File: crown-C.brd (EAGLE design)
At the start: 57.8 x 50.8 mm, 85 parts

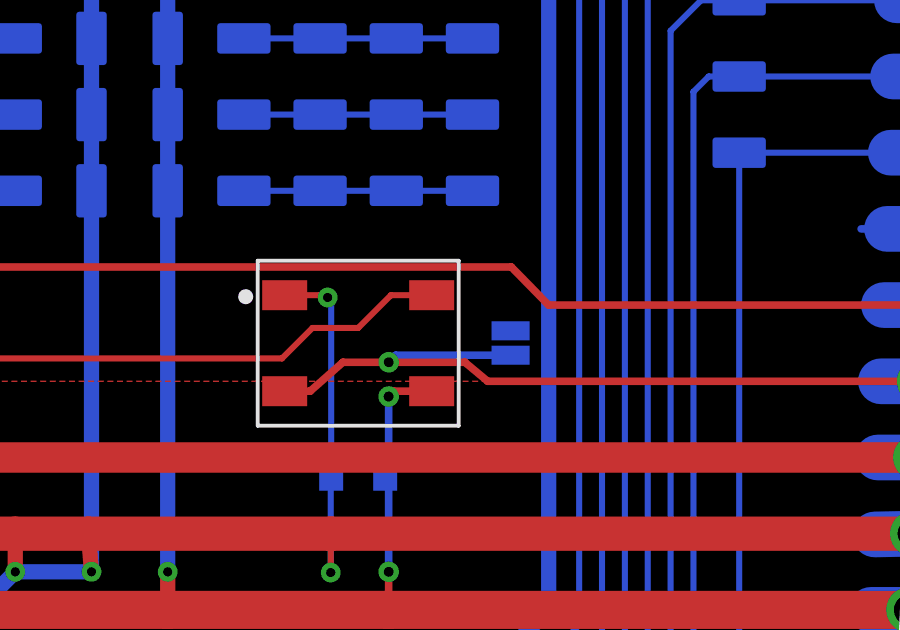
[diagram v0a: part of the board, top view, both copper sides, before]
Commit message: forgot a connection on skip-smd bits
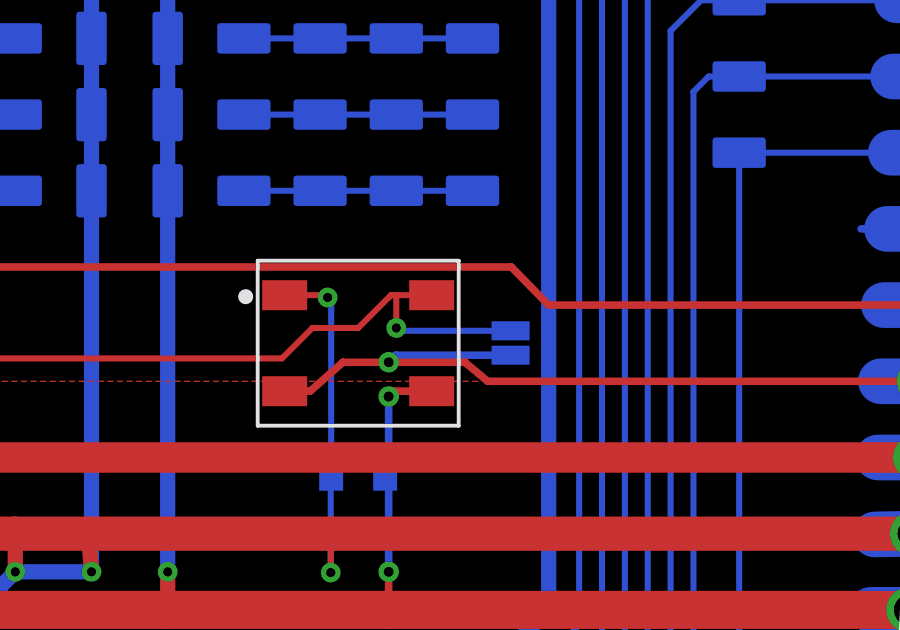
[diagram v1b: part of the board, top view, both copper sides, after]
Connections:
- net N$10: now also SKIP-SMD2.2
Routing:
- net N$10: track 28.2 -> 33.2 mm, vias 1 -> 2

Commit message: fixed incorrect resistor value
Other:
- board text added: "PIXEL LINE TERMINATION (500 OHM RES)"
- board text removed: "PIXEL LINE TERMINATION (150 OHM RES)"
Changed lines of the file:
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@@
 <text x="12.954" y="16.51" size="0.762" layer="22" font="vector" ratio="15" rot="MR90" align="bottom-center">PIXEL LINE
 TERMINATION
-(150 OHM RES)</text>
+(500 OHM RES)</text>
 <text x="4.572" y="7.62" size="0.762" layer="22" font="vector" ratio="15" rot="MR0" align="center-right">GND</text>
 <text x="4.572" y="5.08" size="0.762" layer="22" font="vector" ratio="15" rot="MR0" align="center-right">VBAT</text>
